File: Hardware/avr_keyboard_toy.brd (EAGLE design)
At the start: 22.9 x 47.6 mm, 16 parts, among them CN1 MISC, J1 TFT, J2 I2C, J3 MISC2, SW1 SPST_TACT-EVQQ2, U1 ATMEGA328P-AU

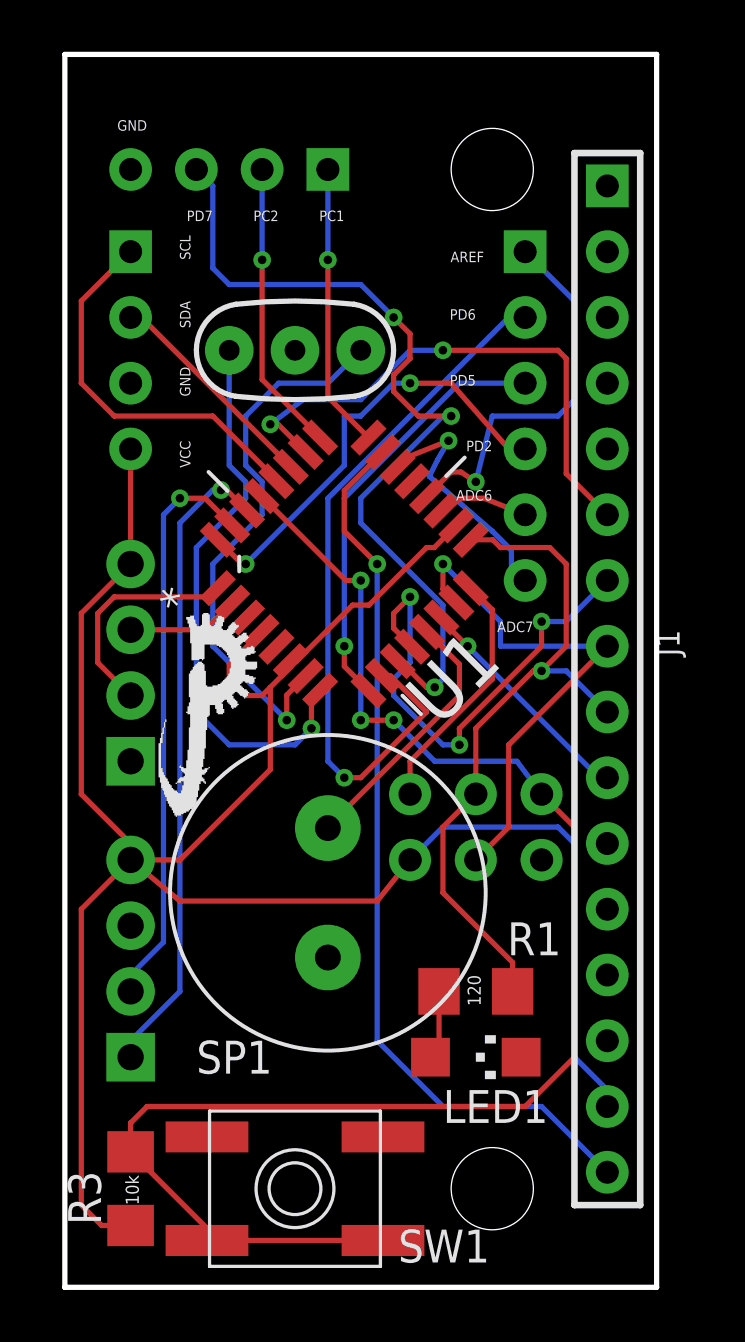
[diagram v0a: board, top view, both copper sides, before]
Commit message: Made the board a bit more configurable Added jumpers to allow me to configure one board for one display board, and another one for a different one.
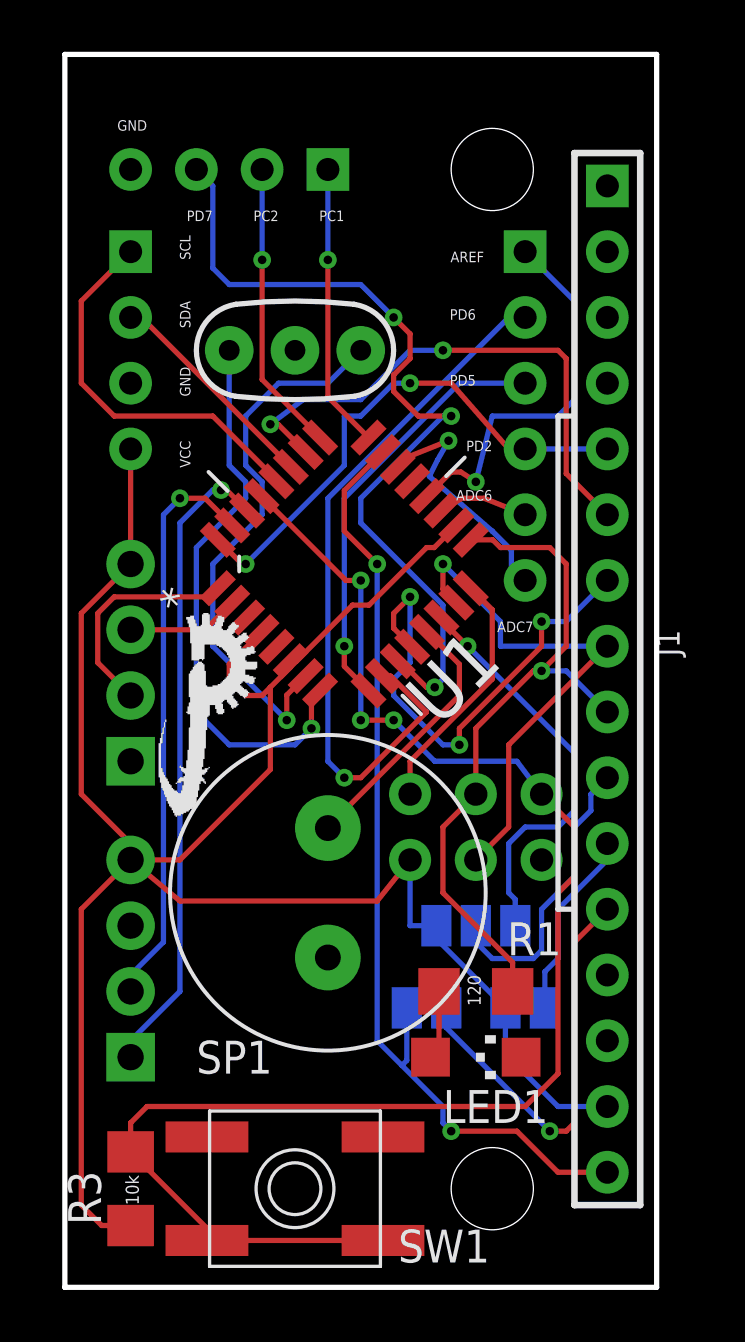
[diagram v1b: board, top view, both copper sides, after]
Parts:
- added BL_JP, GND_JP: (no value), jumper:SJ
- added SS_VCC_JP: (no value), jumper:SJ_2
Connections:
- new net BL_JP: BL_JP.2, J1.11
- new net GND_JP: GND_JP.2, J1.12
- new net SS_VCC_JP: J1.10, SS_VCC_JP.2
- net PD2: now also J1.5
- net SS: now also SS_VCC_JP.3; no longer J1.10
- net TFT_EN: now also GND_JP.1
- net VCC: now also BL_JP.1, SS_VCC_JP.1
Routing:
- net GND_JP: track 0.00 -> 16.3 mm, vias 0 -> 1
- net SS_VCC_JP: track 0.00 -> 11.9 mm
- net BL_JP: track 0.00 -> 7.35 mm
- net SS: track 9.03 -> 15.9 mm
- net VCC: track 88.0 -> 84.6 mm
- net PD2: track 17.4 -> 20.6 mm
- net TFT_EN: track 34.9 -> 37.6 mm, vias 1 -> 2
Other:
- board text added: "SS"
